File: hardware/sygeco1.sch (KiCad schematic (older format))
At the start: 16 parts, among them J1 SSD1306_module, J2 AVR-ISP-6, SW1 SW_Push_DPDT, SW2 SW_Push_DPDT, U1 ATtiny85-20PU

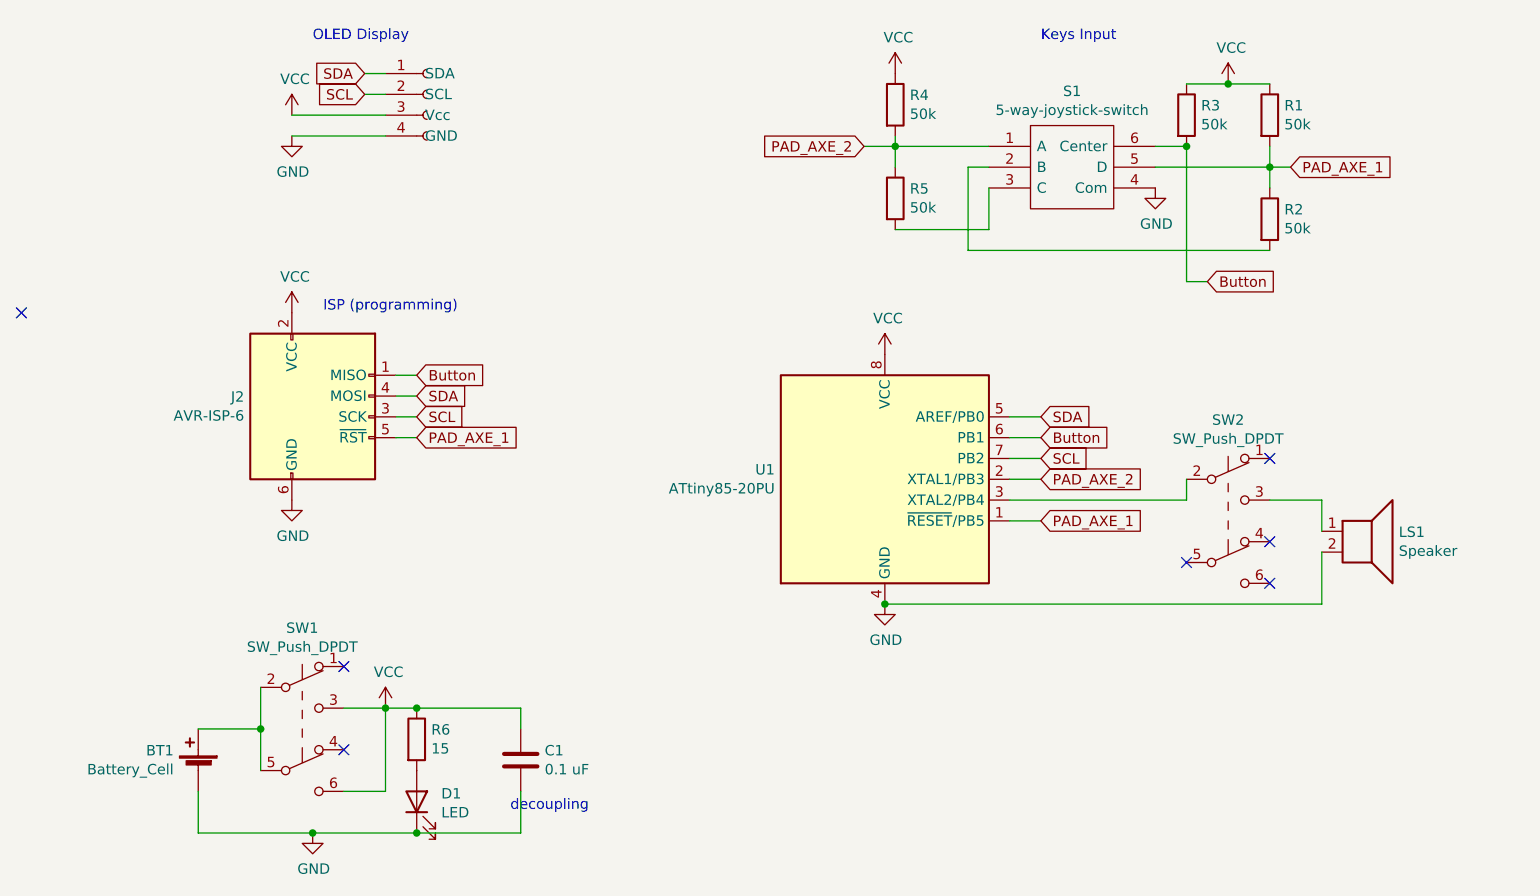
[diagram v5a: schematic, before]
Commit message: few fixes * sch: fix typo (axe -> axis) * reduce battery holder hole size now that i have the actual device to check * some routing cleaning * contrary to my expectation, the isp header works as is, even with my large connector
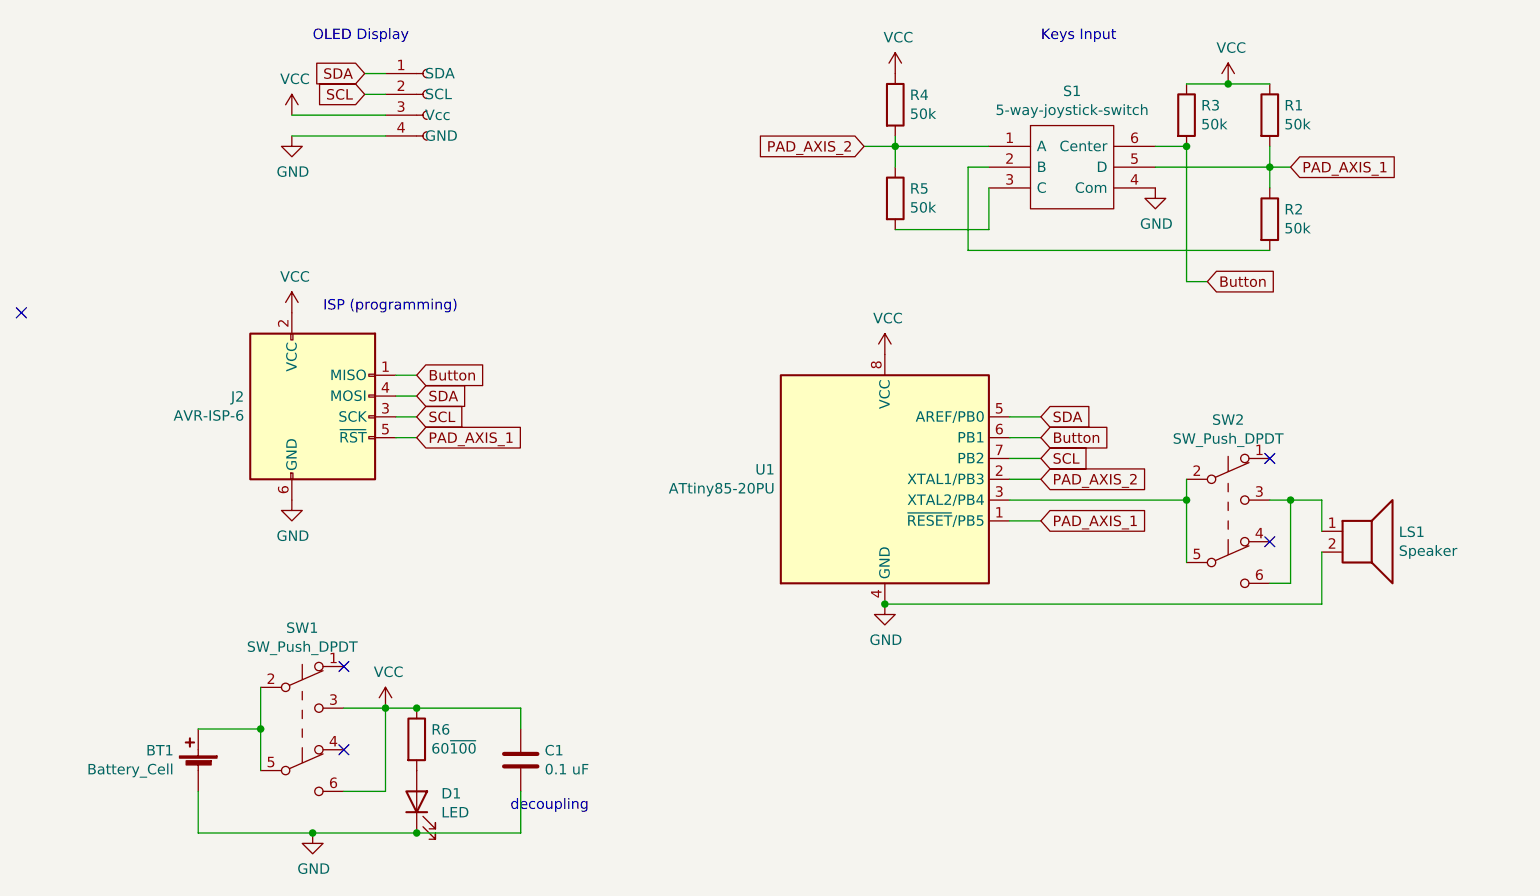
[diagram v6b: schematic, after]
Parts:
- R6: value 15 -> 60~100
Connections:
- net at SW2.2 (B), U1.3 (XTAL2/PB4): now also SW2.5 (B)
- net at LS1.1, SW2.3 (C): now also SW2.6 (C)
- net PAD_AXE_1 renamed PAD_AXIS_1
- net PAD_AXE_2 renamed PAD_AXIS_2
- no-connect marks 7 -> 5
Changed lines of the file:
@@
 $EndComp
 Text GLabel 5350 3200 2    50   Input ~ 0
-PAD_AXE_1
+PAD_AXIS_1
 Text GLabel 5350 3000 2    50   Input ~ 0
-PAD_AXE_2
+PAD_AXIS_2
 Wire Wire Line
 	5350 3000 5200 3000
@@
 $EndComp
 Text GLabel 4500 1400 0    50   Input ~ 0
-PAD_AXE_2
+PAD_AXIS_2
 $Comp
 L power:VCC #PWR0107
@@
 	5900 1400 6050 1400
 Text GLabel 6550 1500 2    50   Input ~ 0
-PAD_AXE_1
+PAD_AXIS_1
 $Comp
 L Device:R R1
@@
 $EndComp
 Wire Wire Line
-	6450 3100 6700 3100
+	6450 3100 6550 3100
 Wire Wire Line
 	6700 3100 6700 3250
@@
 NoConn ~ 2000 4300
 NoConn ~ 6450 2900
-NoConn ~ 6450 3300
 NoConn ~ 450  2200
-NoConn ~ 6450 3500
 Wire Wire Line
 	6700 3350 6700 3600
@@
 	-1   0    0    -1
 $EndComp
-NoConn ~ 6050 3400
 $Comp
 L Connector:AVR-ISP-6 J2
@@
 $EndComp
 Text GLabel 2350 2800 2    50   Input ~ 0
-PAD_AXE_1
+PAD_AXIS_1
 Text GLabel 2350 2700 2    50   Input ~ 0
 SCL
@@
 P 2350 4250
 F 0 "R6" H 2420 4296 50  0000 L CNN
-F 1 "15" H 2420 4205 50  0000 L CNN
+F 1 "60~100" H 2420 4205 50  0000 L CNN
 F 2 "Resistor_SMD:R_1206_3216Metric" V 2280 4250 50  0001 C CNN
 F 3 "~" H 2350 4250 50  0001 C CNN
@@
 	1    0    0    -1
 $EndComp
+NoConn ~ 6450 3300
+Wire Wire Line
+	6450 3500 6550 3500
+Wire Wire Line
+	6550 3500 6550 3100
+Connection ~ 6550 3100
+Wire Wire Line
+	6550 3100 6700 3100
+Wire Wire Line
+	6050 3400 6050 3100
+Connection ~ 6050 3100
 $EndSCHEMATC

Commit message: add mounting holes for the screen
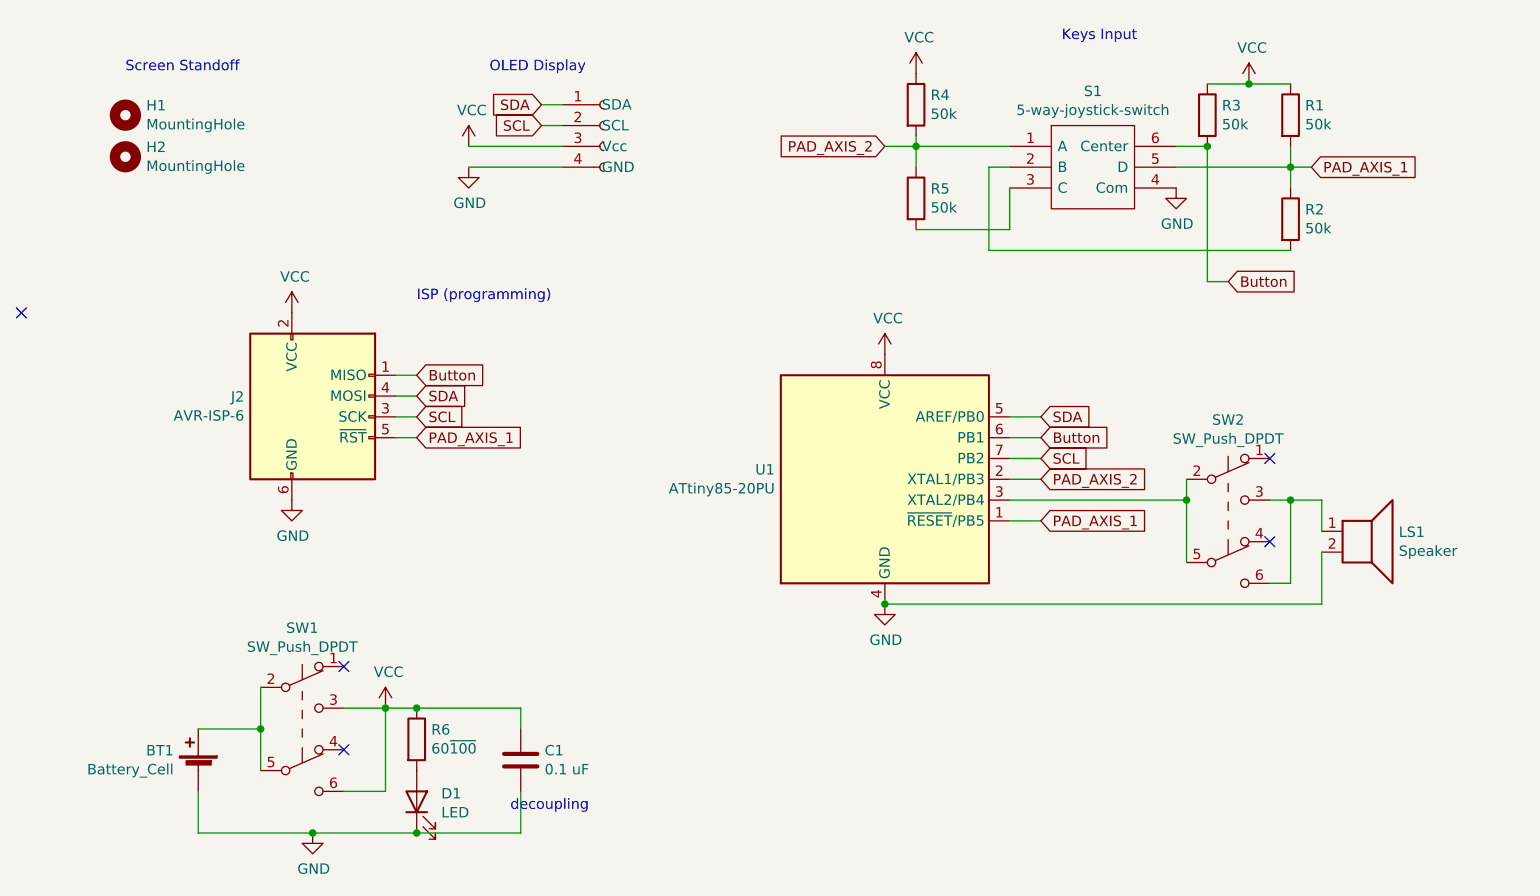
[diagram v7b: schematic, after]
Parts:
- added H1, H2: MountingHole, MountingHole:MountingHole_2.2mm_M2_ISO7380_Pad, symbol Mechanical:MountingHole
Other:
- note added: "Screen Standoff"
- moved on the sheet: R1, R2, R3, R4, R5, S1

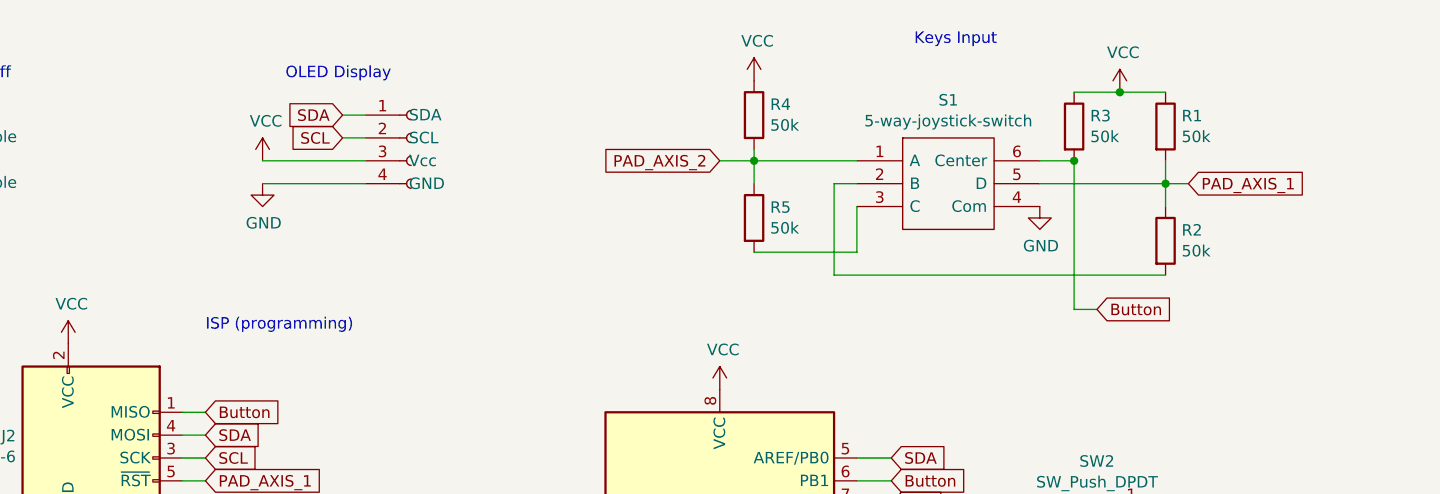
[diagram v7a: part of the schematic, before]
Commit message: Restore original (tinyjoypad) input schematics, with dual resistors and reset pin >= vcc/2
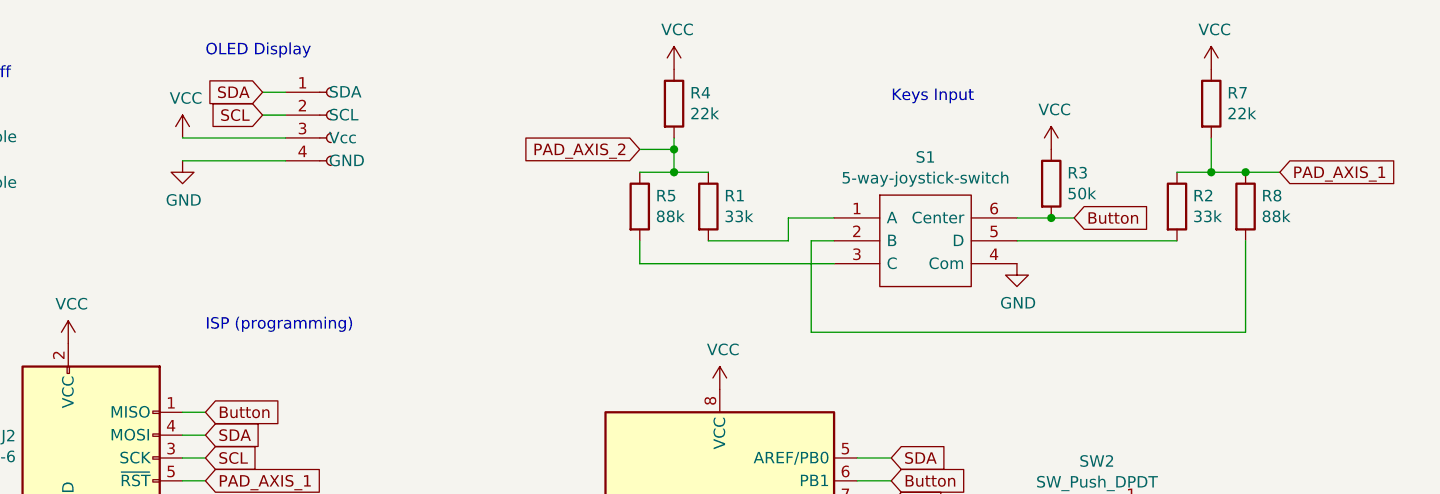
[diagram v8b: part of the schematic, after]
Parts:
- added R7: 22k, Resistor_SMD:R_1206_3216Metric_Pad1.30x1.75mm_HandSolder, symbol Device:R
- added R8: 88k, Resistor_SMD:R_1206_3216Metric_Pad1.30x1.75mm_HandSolder, symbol Device:R
- R1, R2: value 50k -> 33k
- R4: value 50k -> 22k
- R5: value 50k -> 88k
- R6: footprint Resistor_SMD:R_1206_3216Metric -> Resistor_SMD:R_1206_3216Metric_Pad1.30x1.75mm_HandSolder
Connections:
- net PAD_AXIS_1: now also R7.2, R8.1; no longer R1.2, S1.5 (D)
- net PAD_AXIS_2: now also R1.1; no longer S1.1 (A)
- net VCC: now also R7.1; no longer R1.1
- net at S1.2 (B): now also R8.2; no longer R2.2
- new net: R1.2, S1.1 (A)
- new net: R2.2, S1.5 (D)
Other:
- moved on the sheet: R3, R4, R5, S1
